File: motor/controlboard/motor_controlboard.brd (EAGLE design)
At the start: 47 x 70.8 mm, 27 parts, among them IC1 74AHC1G32DCK

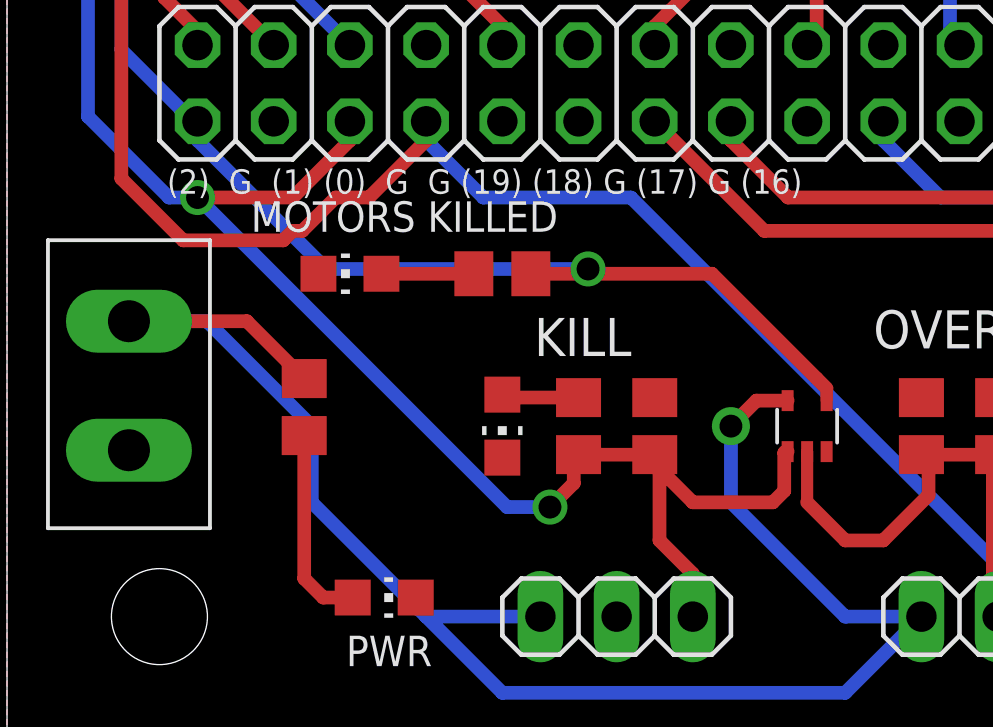
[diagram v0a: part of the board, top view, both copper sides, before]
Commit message: changed trace width for kill switch trace after drc
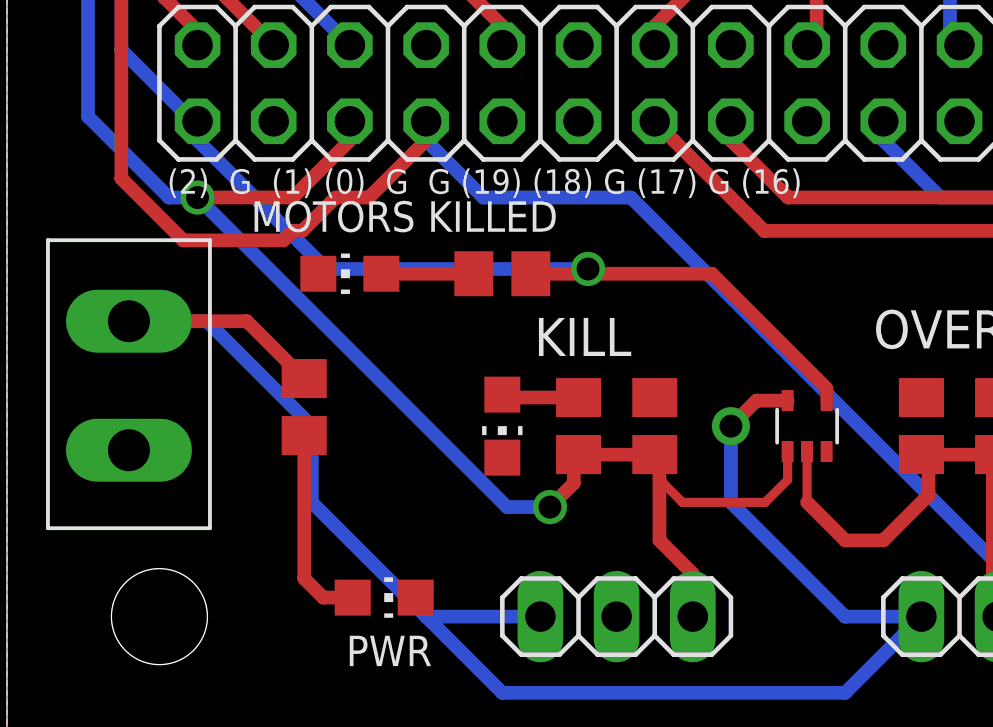
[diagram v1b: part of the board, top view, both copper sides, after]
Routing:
- net KILL: track 84.4 -> 83.5 mm
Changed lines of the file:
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@@
 <?xml version="1.0" encoding="utf-8"?>
 <!DOCTYPE eagle SYSTEM "eagle.dtd">
-<eagle version="8.0.1">
+<eagle version="8.2.0">
 <drawing>
 <settings>
@@
 </class>
 </classes>
-<designrules name="default">
+<designrules name="SeeedStudio_2layer_DRU">
 <description language="de">&lt;b&gt;EAGLE Design Rules&lt;/b&gt;
 &lt;p&gt;
@@
 necessary adjustments and save your customized
 design rules under a new name.</description>
+<description language="zh">&lt;b&gt;Seeed Studio EAGLE Design Rules&lt;/b&gt;
+</description>
 <param name="layerSetup" value="(1*16)"/>
-<param name="mtCopper" value="0.035mm 0.035mm 0.035mm 0.035mm 0.035mm 0.035mm 0.035mm 0.035mm 0.035mm 0.035mm 0.035mm 0.035mm 0.035mm 0.035mm 0.035mm 0.035mm"/>
-<param name="mtIsolate" value="1.5mm 0.15mm 0.2mm 0.15mm 0.2mm 0.15mm 0.2mm 0.15mm 0.2mm 0.15mm 0.2mm 0.15mm 0.2mm 0.15mm 0.2mm"/>
-<param name="mdWireWire" value="8mil"/>
-<param name="mdWirePad" value="8mil"/>
-<param name="mdWireVia" value="8mil"/>
-<param name="mdPadPad" value="8mil"/>
-<param name="mdPadVia" value="8mil"/>
-<param name="mdViaVia" value="8mil"/>
-<param name="mdSmdPad" value="8mil"/>
-<param name="mdSmdVia" value="8mil"/>
-<param name="mdSmdSmd" value="8mil"/>
+<param name="mtCopper" value="0.035mm 0.0175mm 0.035mm 0.035mm 0.035mm 0.035mm 0.035mm 0.035mm 0.035mm 0.035mm 0.035mm 0.035mm 0.035mm 0.035mm 0.0175mm 0.035mm"/>
+<param name="mtIsolate" value="1.5mm 1.1mm 0.2mm 0.15mm 0.2mm 0.15mm 0.2mm 0.15mm 0.2mm 0.15mm 0.2mm 0.15mm 0.2mm 0.15mm 0.2mm"/>
+<param name="mdWireWire" value="6mil"/>
+<param name="mdWirePad" value="6mil"/>
+<param name="mdWireVia" value="6mil"/>
+<param name="mdPadPad" value="6mil"/>
+<param name="mdPadVia" value="6mil"/>
+<param name="mdViaVia" value="6mil"/>
+<param name="mdSmdPad" value="0mil"/>
+<param name="mdSmdVia" value="0mil"/>
+<param name="mdSmdSmd" value="0mil"/>
 <param name="mdViaViaSameLayer" value="8mil"/>
 <param name="mnLayersViaInSmd" value="2"/>
-<param name="mdCopperDimension" value="40mil"/>
-<param name="mdDrill" value="8mil"/>
+<param name="mdCopperDimension" value="10mil"/>
+<param name="mdDrill" value="10mil"/>
 <param name="mdSmdStop" value="0mil"/>
-<param name="msWidth" value="10mil"/>
-<param name="msDrill" value="24mil"/>
-<param name="msMicroVia" value="9.99mm"/>
+<param name="msWidth" value="6mil"/>
+<param name="msDrill" value="12mil"/>
+<param name="msMicroVia" value="12mil"/>
 <param name="msBlindViaRatio" value="0.5"/>
 <param name="rvPadTop" value="0.25"/>
@@
 <param name="rlMinPadBottom" value="10mil"/>
 <param name="rlMaxPadBottom" value="20mil"/>
-<param name="rlMinViaOuter" value="8mil"/>
+<param name="rlMinViaOuter" value="6mil"/>
 <param name="rlMaxViaOuter" value="20mil"/>
-<param name="rlMinViaInner" value="8mil"/>
+<param name="rlMinViaInner" value="6mil"/>
 <param name="rlMaxViaInner" value="20mil"/>
 <param name="rlMinMicroViaOuter" value="4mil"/>
@@
 <param name="psTop" value="-1"/>
 <param name="psBottom" value="-1"/>
-<param name="psFirst" value="-1"/>
+<param name="psFirst" value="0"/>
 <param name="psElongationLong" value="100"/>
 <param name="psElongationOffset" value="100"/>
 <param name="mvStopFrame" value="1"/>
 <param name="mvCreamFrame" value="0"/>
-<param name="mlMinStopFrame" value="4mil"/>
-<param name="mlMaxStopFrame" value="4mil"/>
+<param name="mlMinStopFrame" value="2mil"/>
+<param name="mlMaxStopFrame" value="2mil"/>
 <param name="mlMinCreamFrame" value="0mil"/>
 <param name="mlMaxCreamFrame" value="0mil"/>
-<param name="mlViaStopLimit" value="0mil"/>
+<param name="mlViaStopLimit" value="100mil"/>
 <param name="srRoundness" value="0"/>
 <param name="srMinRoundness" value="0mil"/>
@@
 <param name="checkAngle" value="0"/>
 <param name="checkFont" value="1"/>
-<param name="checkRestrict" value="1"/>
+<param name="checkRestrict" value="0"/>
 <param name="useDiameter" value="13"/>
 <param name="maxErrors" value="50"/>
@@
 <wire x1="19.05" y1="9.2075" x2="19.05" y2="9.21" width="0.4572" layer="1"/>
 <wire x1="21.59" y1="9.2075" x2="21.59" y2="9.21" width="0.4572" layer="1"/>
-<wire x1="21.74875" y1="6.35" x2="21.74875" y2="9.04875" width="0.4572" layer="1"/>
+<wire x1="21.74875" y1="8.382" x2="21.74875" y2="6.35" width="0.4572" layer="1"/>
+<wire x1="21.74875" y1="8.382" x2="21.74875" y2="9.04875" width="0.4572" layer="1"/>
 <wire x1="22.86" y1="5.23875" x2="21.74875" y2="6.35" width="0.4572" layer="1"/>
 <wire x1="22.86" y1="3.81" x2="22.86" y2="5.23875" width="0.4572" layer="1"/>
@@
 <via x="6.35" y="17.78" extent="1-16" drill="0.762"/>
 <via x="18.0975" y="7.46125" extent="1-16" drill="0.762"/>
-<wire x1="21.59" y1="9.21" x2="21.59" y2="8.89" width="0.4572" layer="1"/>
-<wire x1="21.59" y1="8.89" x2="22.86" y2="7.62" width="0.4572" layer="1"/>
-<wire x1="22.86" y1="7.62" x2="25.527" y2="7.62" width="0.4572" layer="1"/>
-<wire x1="25.527" y1="7.62" x2="25.908" y2="8.001" width="0.4572" layer="1"/>
-<wire x1="25.908" y1="9.271" x2="25.908" y2="8.001" width="0.4572" layer="1"/>
-<wire x1="26.02" y1="9.31" x2="25.947" y2="9.31" width="0.4572" layer="1"/>
-<wire x1="25.947" y1="9.31" x2="25.908" y2="9.271" width="0.4572" layer="1"/>
+<wire x1="26.02" y1="9.31" x2="26.02" y2="8.367" width="0.3048" layer="1"/>
+<wire x1="26.02" y1="8.367" x2="25.273" y2="7.62" width="0.3048" layer="1"/>
+<wire x1="25.273" y1="7.62" x2="22.51075" y2="7.62" width="0.3048" layer="1"/>
+<wire x1="22.51075" y1="7.62" x2="21.74875" y2="8.382" width="0.3048" layer="1"/>
 </signal>
 <signal name="OVERRIDE">
@@
 <wire x1="13.97" y1="19.685" x2="15.875" y2="17.78" width="0.4572" layer="16"/>
 <wire x1="13.97" y1="20.32" x2="13.97" y2="19.685" width="0.4572" layer="16"/>
-<wire x1="26.67" y1="9.31" x2="26.67" y2="7.62" width="0.4064" layer="1"/>
 <wire x1="26.67" y1="7.62" x2="27.94" y2="6.35" width="0.4572" layer="1"/>
 <wire x1="27.94" y1="6.35" x2="29.21" y2="6.35" width="0.4572" layer="1"/>
@@
 <wire x1="30.718125" y1="7.858125" x2="30.718125" y2="8.971875" width="0.4572" layer="1"/>
 <wire x1="30.718125" y1="8.971875" x2="30.48" y2="9.21" width="0.4572" layer="1"/>
+<wire x1="26.67" y1="9.31" x2="26.67" y2="7.62" width="0.3048" layer="1"/>
 </signal>
 <signal name="N$1">

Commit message: Updated board May 28
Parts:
- moved C_(23) 4.91 mm to (46.5, 32.4)
- moved F_(3) 4.62 mm to (46.4, 60.1)
- moved E_(6) 4.49 mm to (46.4, 50.7)
- moved B_(21) 4.47 mm to (46.5, 21.7)
- moved A_(20) 4.24 mm to (46.4, 11.7)
- moved D_(9) 4.19 mm to (46.4, 41.4)
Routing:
- net SIG_10: track 44.7 -> 48.6 mm
- net SIG_1: track 44.4 -> 47.6 mm
- net SIG_7: track 31.7 -> 34.6 mm
- net SIG_4: track 60.1 -> 62.9 mm
- net SIG_5: track 69.7 -> 72.5 mm
- net KILL: track 83.5 -> 84.4 mm
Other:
- board size 47 x 70.8 mm -> 50.8 x 76.3 mm
- board text added: "(20)"
- board text added: "(21)"
- board text added: "(23)"
- board text added: "(3)"
- board text added: "(6)"
- board text added: "(9)"
- board text added: "ALL MOUNTING HOLES ARE 1/8" IN DIAMETER. THESE MOUNTING HOLES ARE 1/8" AWAY FROM THE EDGES W/ RESPECT TO X AND Y"
